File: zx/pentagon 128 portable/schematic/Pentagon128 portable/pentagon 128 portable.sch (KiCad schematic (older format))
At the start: 0 parts

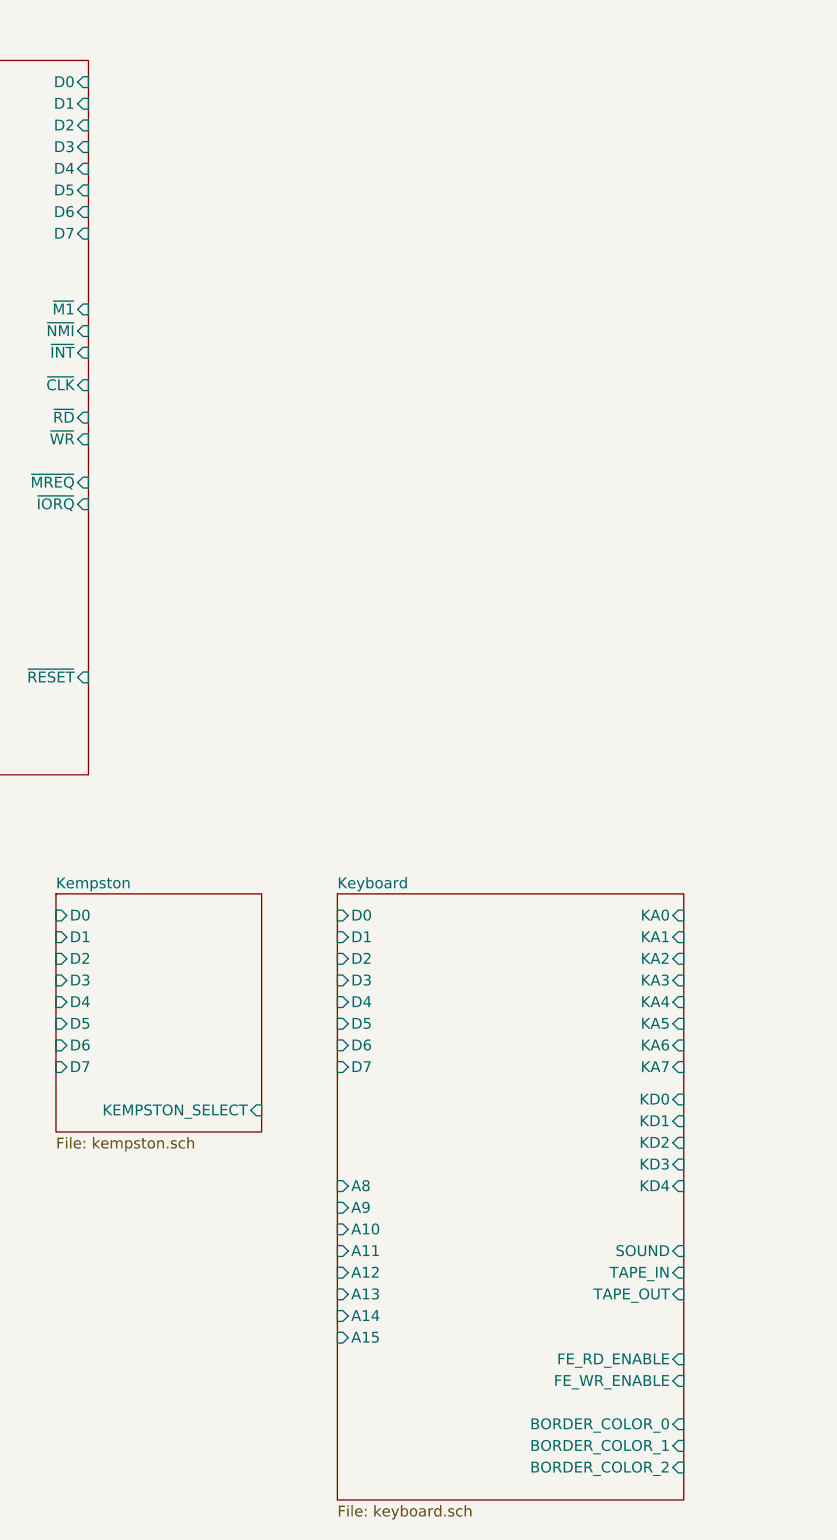
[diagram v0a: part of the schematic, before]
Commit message: reorganizing. finished ram and keyboard, updated z80
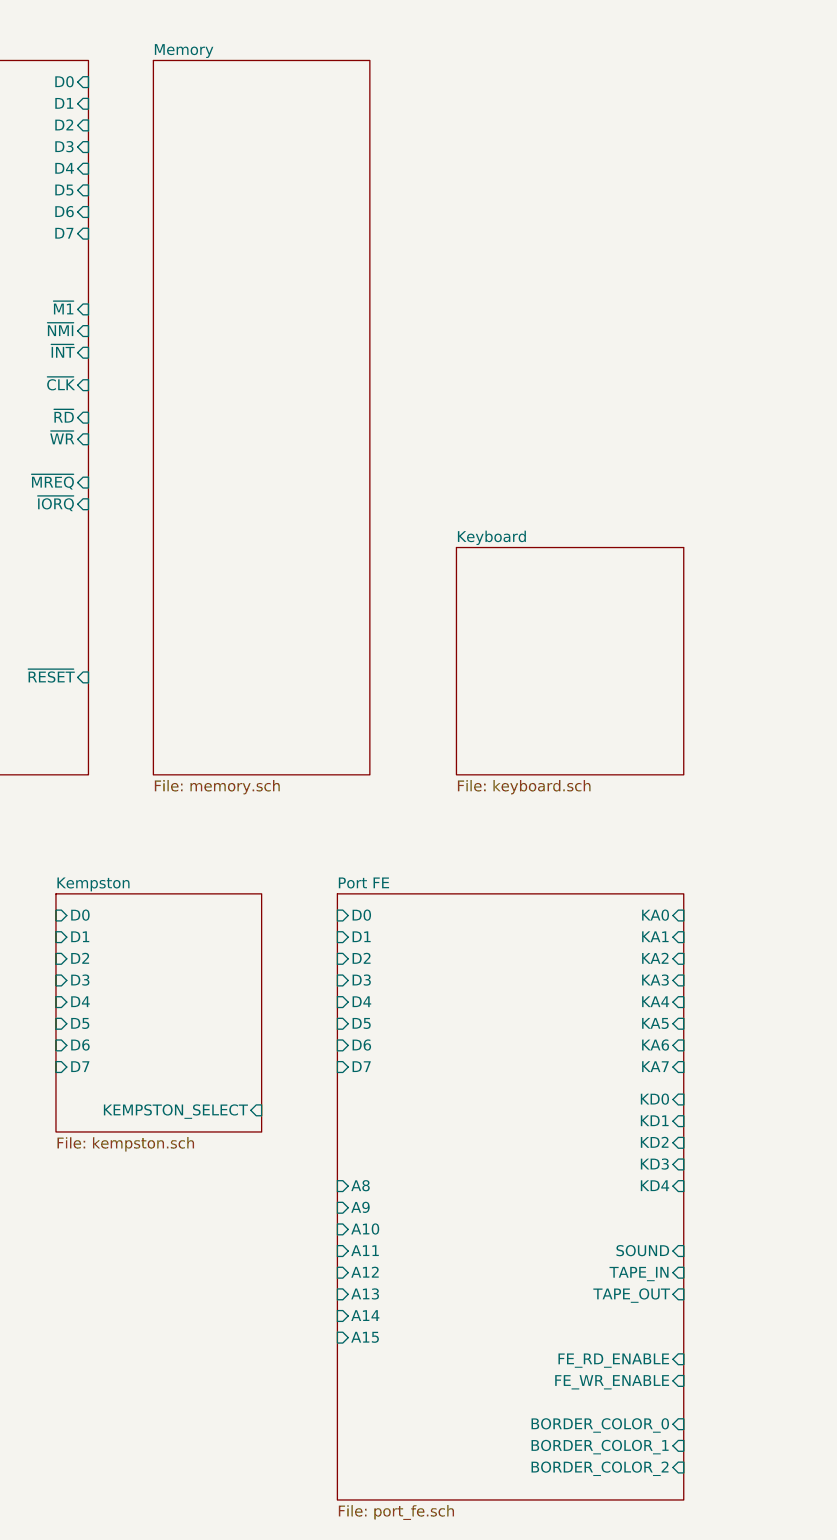
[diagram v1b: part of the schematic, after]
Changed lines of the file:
@@
 $Descr A4 11693 8268
 encoding utf-8
-Sheet 1 6
+Sheet 1 8
 Title ""
 Date ""
@@
 S 3650 4750 1600 2800
 U 5F5BE176
-F0 "Keyboard" 50
-F1 "keyboard.sch" 50
+F0 "Port FE" 50
+F1 "port_fe.sch" 50
 F2 "A8" I L 3650 6100 50
 F3 "A9" I L 3650 6200 50
@@
 F38 "BORDER_COLOR_2" I R 5250 7400 50
 $EndSheet
+$Sheet
+S 2800 900  1000 3300
+U 5F6C4F45
+F0 "Memory" 50
+F1 "memory.sch" 50
+$EndSheet
+$Sheet
+S 4200 3150 1050 1050
+U 5F6C4FE3
+F0 "Keyboard" 50
+F1 "keyboard.sch" 50
+$EndSheet
 $EndSCHEMATC

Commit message: some reordering in the main project
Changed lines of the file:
@@
 $Descr A4 11693 8268
 encoding utf-8
-Sheet 1 8
+Sheet 1 14
 Title ""
 Date ""
@@
 S 900  900  1600 3300
 U 5F4A5B2D
-F0 "SPU" 50
+F0 "CPU" 50
 F1 "CPU.sch" 50
 F2 "A14" I L 900 2400 50
@@
 $EndSheet
 $Sheet
+S 2800 900  1000 3300
+U 5F6C4F45
+F0 "Memory" 50
+F1 "memory.sch" 50
+F2 "RAM_PG0" I R 3800 1000 50
+F3 "RAM_PG1" I R 3800 1100 50
+F4 "RAM_PG2" I R 3800 1200 50
+F5 "RAM_PG3" I R 3800 1300 50
+F6 "RAM_PG4" I R 3800 1400 50
+F7 "ROM_PG2" I R 3800 2250 50
+F8 "ROM_PG1" I R 3800 2150 50
+F9 "ROM_PG0" I R 3800 2050 50
+F10 "~ROM_OE" I R 3800 2550 50
+F11 "~ROM_CE" I R 3800 2450 50
+F12 "~ROM_WE" I R 3800 2650 50
+F13 "~RAM_CE" I R 3800 1600 50
+F14 "~RAM_OE" I R 3800 1700 50
+F15 "~RAM_WE" I R 3800 1800 50
+F16 "A13" I L 2800 2300 50
+F17 "A11" I L 2800 2100 50
+F18 "A10" I L 2800 2000 50
+F19 "A9" I L 2800 1900 50
+F20 "A8" I L 2800 1800 50
+F21 "A12" I L 2800 2200 50
+F22 "A7" I L 2800 1700 50
+F23 "A6" I L 2800 1600 50
+F24 "A5" I L 2800 1500 50
+F25 "A4" I L 2800 1400 50
+F26 "A3" I L 2800 1300 50
+F27 "A2" I L 2800 1200 50
+F28 "A1" I L 2800 1100 50
+F29 "A0" I L 2800 1000 50
+F30 "D7" I L 2800 3750 50
+F31 "D6" I L 2800 3650 50
+F32 "D5" I L 2800 3550 50
+F33 "D4" I L 2800 3450 50
+F34 "D3" I L 2800 3350 50
+F35 "D2" I L 2800 3250 50
+F36 "D1" I L 2800 3150 50
+F37 "D0" I L 2800 3050 50
+$EndSheet
+$Sheet
+S 4100 1500 950  2700
+U 5F6C4FE3
+F0 "Keyboard" 50
+F1 "keyboard.sch" 50
+F2 "A0" I R 5050 1650 50
+F3 "~IORQ" I R 5050 1750 50
+F4 "~RD" I R 5050 1850 50
+F5 "D0" I L 4100 1600 50
+F6 "D1" I L 4100 1700 50
+F7 "D2" I L 4100 1800 50
+F8 "D3" I L 4100 1900 50
+F9 "D4" I L 4100 2000 50
+F10 "A8" I L 4100 2350 50
+F11 "A9" I L 4100 2450 50
+F12 "A10" I L 4100 2550 50
+F13 "A11" I L 4100 2650 50
+F14 "A12" I L 4100 2750 50
+F15 "A13" I L 4100 2850 50
+F16 "A14" I L 4100 2950 50
+F17 "A15" I L 4100 3050 50
+$EndSheet
+$Sheet
+S 900  6750 1000 950
+U 5F64EC48
+F0 "power" 50
+F1 "power.sch" 50
+$EndSheet
+$Sheet
 S 3650 4750 1600 2800
 U 5F5BE176
 F0 "Port FE" 50
 F1 "port_fe.sch" 50
-F2 "A8" I L 3650 6100 50
-F3 "A9" I L 3650 6200 50
-F4 "A10" I L 3650 6300 50
-F5 "A11" I L 3650 6400 50
-F6 "A12" I L 3650 6500 50
-F7 "A13" I L 3650 6600 50
-F8 "A14" I L 3650 6700 50
-F9 "A15" I L 3650 6800 50
-F10 "KA7" I R 5250 5550 50
-F11 "KA6" I R 5250 5450 50
-F12 "KA5" I R 5250 5350 50
-F13 "KA4" I R 5250 5250 50
-F14 "KA3" I R 5250 5150 50
-F15 "KA2" I R 5250 5050 50
-F16 "KA1" I R 5250 4950 50
-F17 "KA0" I R 5250 4850 50
-F18 "FE_RD_ENABLE" I R 5250 6900 50
-F19 "KD4" I R 5250 6100 50
-F20 "KD3" I R 5250 6000 50
-F21 "KD2" I R 5250 5900 50
-F22 "KD1" I R 5250 5800 50
-F23 "KD0" I R 5250 5700 50
-F24 "D7" I L 3650 5550 50
-F25 "D5" I L 3650 5350 50
-F26 "D6" I L 3650 5450 50
-F27 "D4" I L 3650 5250 50
-F28 "D3" I L 3650 5150 50
-F29 "D2" I L 3650 5050 50
-F30 "D1" I L 3650 4950 50
-F31 "D0" I L 3650 4850 50
-F32 "TAPE_IN" I R 5250 6500 50
-F33 "FE_WR_ENABLE" I R 5250 7000 50
-F34 "SOUND" I R 5250 6400 50
-F35 "TAPE_OUT" I R 5250 6600 50
-F36 "BORDER_COLOR_0" I R 5250 7200 50
-F37 "BORDER_COLOR_1" I R 5250 7300 50
-F38 "BORDER_COLOR_2" I R 5250 7400 50
-$EndSheet
-$Sheet
-S 2800 900  1000 3300
-U 5F6C4F45
-F0 "Memory" 50
-F1 "memory.sch" 50
-$EndSheet
-$Sheet
-S 4200 3150 1050 1050
-U 5F6C4FE3
-F0 "Keyboard" 50
-F1 "keyboard.sch" 50
+F2 "FE_RD_ENABLE" I R 5250 6900 50
+F3 "D7" I L 3650 5550 50
+F4 "D5" I L 3650 5350 50
+F5 "D6" I L 3650 5450 50
+F6 "D4" I L 3650 5250 50
+F7 "D3" I L 3650 5150 50
+F8 "D2" I L 3650 5050 50
+F9 "D1" I L 3650 4950 50
+F10 "D0" I L 3650 4850 50
+F11 "TAPE_IN" I R 5250 6500 50
+F12 "FE_WR_ENABLE" I R 5250 7000 50
+F13 "SOUND" I R 5250 6400 50
+F14 "TAPE_OUT" I R 5250 6600 50
+F15 "BORDER_COLOR_0" I R 5250 7200 50
+F16 "BORDER_COLOR_1" I R 5250 7300 50
+F17 "BORDER_COLOR_2" I R 5250 7400 50
+$EndSheet
+$Sheet
+S 6000 3400 1500 2600
+U 5F748573
+F0 "peripheral" 50
+F1 "peripheral.sch" 50
 $EndSheet
 $EndSCHEMATC
